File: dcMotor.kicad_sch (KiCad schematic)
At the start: 121 parts, among them J1 USB_C_Receptacle_USB2.0_16P, J2 USB_C_Receptacle_USB2.0_16P, J3 Conn_ST_STDC14, J6 Conn_01x02_Pin, J7 Conn_01x04_Pin, J8 Conn_01x06_Pin, Q1 AO3400A, SW1 SW_Push, SW2 SW_Push, U1 LMR54406DBVR, U10 MCP6561-OT, U11 NUCLEO-L432KC, U2 NCP718ASNADJT1G, U3 NCP718ASNADJT1G, U5 TLV9152IDR, U6 ER_OLEDM0.91_1x-I2C, U7 STM32G431CBTx, U8 LTH-301-05, U9 DRV8231ADDA

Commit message: wip
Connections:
- net +3.3V: now also J7.2 (Pin_2)
- net GND: now also J7.1 (Pin_1)
- net I2C2_SCL: now also J7.3 (Pin_3)
- net I2C2_SDA: now also J7.4 (Pin_4)
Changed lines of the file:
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@@
 	(wire
 		(pts
+			(xy 160.02 59.69) (xy 162.56 59.69)
+		)
+		(stroke
+			(width 0)
+			(type default)
+		)
+	)
+	(wire
+		(pts
 			(xy 294.64 64.77) (xy 304.8 64.77)
 		)
@@
 	(wire
 		(pts
+			(xy 160.02 54.61) (xy 171.45 54.61)
+		)
+		(stroke
+			(width 0)
+			(type default)
+		)
+	)
+	(wire
+		(pts
 			(xy 95.25 250.19) (xy 109.22 250.19)
 		)
@@
 	(wire
 		(pts
+			(xy 160.02 57.15) (xy 170.18 57.15)
+		)
+		(stroke
+			(width 0)
+			(type default)
+		)
+	)
+	(wire
+		(pts
 			(xy 257.81 158.75) (xy 242.57 158.75)
 		)
@@
 	(wire
 		(pts
+			(xy 160.02 52.07) (xy 171.45 52.07)
+		)
+		(stroke
+			(width 0)
+			(type default)
+		)
+	)
+	(wire
+		(pts
 			(xy 81.28 39.37) (xy 91.44 39.37)
 		)
@@
 		)
 	)
+	(label "I2C2_SCL"
+		(at 171.45 54.61 180)
+		(effects
+			(font
+				(size 1.27 1.27)
+			)
+			(justify right bottom)
+		)
+	)
 	(label "SWCLK"
 		(at 257.81 173.99 180)
@@
 		)
 	)
+	(label "I2C2_SDA"
+		(at 171.45 52.07 180)
+		(effects
+			(font
+				(size 1.27 1.27)
+			)
+			(justify right bottom)
+		)
+	)
 	(label "TIM1_CH1"
 		(at 330.2 149.86 0)
@@
 	(symbol
 		(lib_id "Connector:Conn_01x04_Pin")
-		(at 154.94 54.61 0)
+		(at 154.94 57.15 0)
+		(mirror x)
 		(unit 1)
 		(body_style 1)
@@
 		(in_pos_files yes)
 		(dnp yes)
-		(fields_autoplaced yes)
 		(property "Reference" "J7"
-			(at 155.575 46.99 0)
+			(at 155.575 64.77 0)
 			(show_name no)
 			(do_not_autoplace no)
@@
 		)
 		(property "Value" "Conn_01x04_Pin"
-			(at 155.575 49.53 0)
+			(at 155.575 62.23 0)
 			(show_name no)
 			(do_not_autoplace no)
@@
 		)
 		(property "Footprint" "Connector_PinHeader_2.54mm:PinHeader_1x04_P2.54mm_Vertical"
-			(at 154.94 54.61 0)
+			(at 154.94 57.15 0)
 			(hide yes)
 			(show_name no)
@@
 		)
 		(property "Datasheet" "https://jlc-prod-smt.oss-eu-central-1.aliyuncs.com/smtDataManualFile/8590908656076869632-C7430360.pdf?response-content-disposition=attachment%3B%20filename%3DC7430360.pdf%3B%20filename%2A%3DUTF-8%27%27C7430360.pdf&x-oss-date=20260803T060238Z&x-oss-expires=1800&x-oss-security-token=CAISgAN1q6Ft5B2yfSjIr5mMDMrQ3ugT1IisQ0KFpVMBWrtIjbbCoDz2IHhMdHJsAOodtv0%2FmmhT6PkclqRLcbhpcmfjV%2BZHzLB8qYV161ZV4J7b16cNrbH4M4H6aXeirtuwDsz9SNTCALjPD3nPii50x5bjaDymRCbLGJaViJlhHLN1Ow6jdmhpCctxLAlvo9NgFxm3D%2Fu2NQPwiWf9FVdhvhEG6Vly8qOi2MaRmFy8yFTx0b0SvJ%2BjYMrmPctoN9JnSdC5mfdzau3a1TJ84gRD0a5wkaVA1zbDs5bfISEIuUzebreLqY03dV4mOvdqIcMe8qigz88fk%2FfIioH6xyxKOexoSCnFTOiiupCcQLPyao9jLu6iayqViY7QaIOTqQohZmkAMwVOasAsI3Ngh4zF97Qt0cVNkXO9gWfLI8DtuMleWorKE09jitHD0eS19jklBdzSlusJRAJJUVBflCeKEaRNSAd3WGhEfM2%2BBt4QT30w5N2u00S8OSMIzVToo6KWD5sagAFvYbpT7M4nKzV9x9nG0KVt6L9PAQwcrMXPLAqBWLfjjl5RjllW3eVSTNXt%2F6qUNa4JzQr3WbjAO3ylgIsIr1rmH1qmomnc5ro9zTqD80vC%2BHI%2B1cBZ6acWZAaNL8CKJQhHlU474BssQ3TqMWqi0fbuUZIeUyi0gR7g0jSOj3oNhSAA&x-oss-signature-version=OSS4-HMAC-SHA256&x-oss-credential=STS.NZ9Gpd372cJGAd4ASTV4dbsiB%2F20260803%2Feu-central-1%2Foss%2Faliyun_v4_request&x-oss-signature=589712091c6788fe5c51930447157b69597e4cec471ecd001fa8bdaaec699515"
-			(at 154.94 54.61 0)
+			(at 154.94 57.15 0)
 			(hide yes)
 			(show_name no)
@@
 		)
 		(property "Description" "Generic connector, single row, 01x04, script generated"
-			(at 154.94 54.61 0)
+			(at 154.94 57.15 0)
 			(hide yes)
 			(show_name no)
@@
 		)
 		(property "LCSC Part #" "C7430360"
-			(at 154.94 54.61 0)
+			(at 154.94 57.15 0)
 			(hide yes)
 			(show_name no)
@@
 		)
 		(property "FT Rotation Offset" "90"
-			(at 154.94 54.61 0)
+			(at 154.94 57.15 0)
 			(hide yes)
 			(show_name no)
@@
 	(symbol
 		(lib_id "power:GND")
+		(at 162.56 59.69 90)
+		(unit 1)
+		(body_style 1)
+		(exclude_from_sim no)
+		(in_bom yes)
+		(on_board yes)
+		(in_pos_files yes)
+		(dnp no)
+		(property "Reference" "#PWR0100"
+			(at 168.91 59.69 0)
+			(hide yes)
+			(show_name no)
+			(do_not_autoplace no)
+			(effects
+				(font
+					(size 1.27 1.27)
+				)
+			)
+		)
+		(property "Value" "GND"
+			(at 166.37 59.69 0)
+			(show_name no)
+			(do_not_autoplace no)
+			(effects
+				(font
+					(size 1.27 1.27)
+				)
+			)
+		)
+		(property "Footprint" ""
+			(at 162.56 59.69 0)
+			(hide yes)
+			(show_name no)
+			(do_not_autoplace no)
+			(effects
+				(font
+					(size 1.27 1.27)
+				)
+			)
+		)
+		(property "Datasheet" ""
+			(at 162.56 59.69 0)
+			(hide yes)
+			(show_name no)
+			(do_not_autoplace no)
+			(effects
+				(font
+					(size 1.27 1.27)
+				)
+			)
+		)
+		(property "Description" "Power symbol creates a global label with name \"GND\" , ground"
+			(at 162.56 59.69 0)
+			(hide yes)
+			(show_name no)
+			(do_not_autoplace no)
+			(effects
+				(font
+					(size 1.27 1.27)
+				)
+			)
+		)
+		(pin "1"
+		)
+		(instances
+			(project "dcMotor"
+				(path "/cdbcf673-237a-45f1-99a3-f4d168bf6e2e"
+					(reference "#PWR0100")
+					(unit 1)
+				)
+			)
+		)
+	)
+	(symbol
+		(lib_id "power:GND")
 		(at 196.85 24.13 90)
 		(unit 1)
@@
 					(unit 1)
 				)
+			)
+		)
+	)
+	(symbol
+		(lib_id "power:+3.3V")
+		(at 170.18 57.15 270)
+		(unit 1)
+		(body_style 1)
+		(exclude_from_sim no)
+		(in_bom yes)
+		(on_board yes)
+		(in_pos_files yes)
+		(dnp no)
+		(property "Reference" "#PWR0101"
+			(at 166.37 57.15 0)
+			(hide yes)
+			(show_name no)
+			(do_not_autoplace no)
+			(effects
+				(font
+					(size 1.27 1.27)
+				)
+			)
+		)
+		(property "Value" "+3.3V"
+			(at 173.99 57.15 0)
+			(show_name no)
+			(do_not_autoplace no)
+			(effects
+				(font
+					(size 1.27 1.27)
+				)
+			)
+		)
+		(property "Footprint" ""
+			(at 170.18 57.15 0)
+			(hide yes)
+			(show_name no)
+			(do_not_autoplace no)
+			(effects
+				(font
+					(size 1.27 1.27)
+				)
+			)
+		)
+		(property "Datasheet" ""
+			(at 170.18 57.15 0)
+			(hide yes)
+			(show_name no)
+			(do_not_autoplace no)
+			(effects
+				(font
+					(size 1.27 1.27)
+				)
+			)
+		)
+		(property "Description" "Power symbol creates a global label with name \"+3.3V\""
+			(at 170.18 57.15 0)
+			(hide yes)
+			(show_name no)
+			(do_not_autoplace no)
+			(effects
+				(font
+					(size 1.27 1.27)
+				)
+			)
+		)
+		(pin "1"
+		)
+		(instances
+			(project "dcMotor"
+				(path "/cdbcf673-237a-45f1-99a3-f4d168bf6e2e"
+					(reference "#PWR0101")
+					(unit 1)
+				)

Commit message: cleanup
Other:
- note added: "TIM2 configured in CubeMX as "combined channels" in Encoder Mode to measure Motor Hall Encoder Signals"
- moved on the sheet: C27, C32, C33, D7, J8, NT1, NT2, R25, R26, R30, R31, TP11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

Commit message: cleanup
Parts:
- added C39, C40: 100n, Capacitor_SMD:C_0402_1005Metric, symbol Device:C
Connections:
- net +3.3V: now also C39.2, C40.2
- net GND: now also C39.1, C40.1
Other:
- note added: "more caps than necessary due to "bad" routing"

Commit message: fabrication
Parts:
- U1, U10, U5: now not fitted
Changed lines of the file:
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@@
 		(on_board yes)
 		(in_pos_files yes)
-		(dnp no)
+		(dnp yes)
 		(property "Reference" "U1"
 			(at 52.07 28.702 0)
@@
 		(on_board yes)
 		(in_pos_files yes)
-		(dnp no)
+		(dnp yes)
 		(property "Reference" "U10"
 			(at 374.904 49.53 0)
@@
 		(on_board yes)
 		(in_pos_files yes)
-		(dnp no)
+		(dnp yes)
 		(property "Reference" "U5"
 			(at 116.84 243.332 0)
@@
 		(on_board yes)
 		(in_pos_files yes)
-		(dnp no)
+		(dnp yes)
 		(fields_autoplaced yes)
 		(property "Reference" "U5"
@@
 		(on_board yes)
 		(in_pos_files yes)
-		(dnp no)
+		(dnp yes)
 		(property "Reference" "U5"
 			(at 180.34 243.332 0)

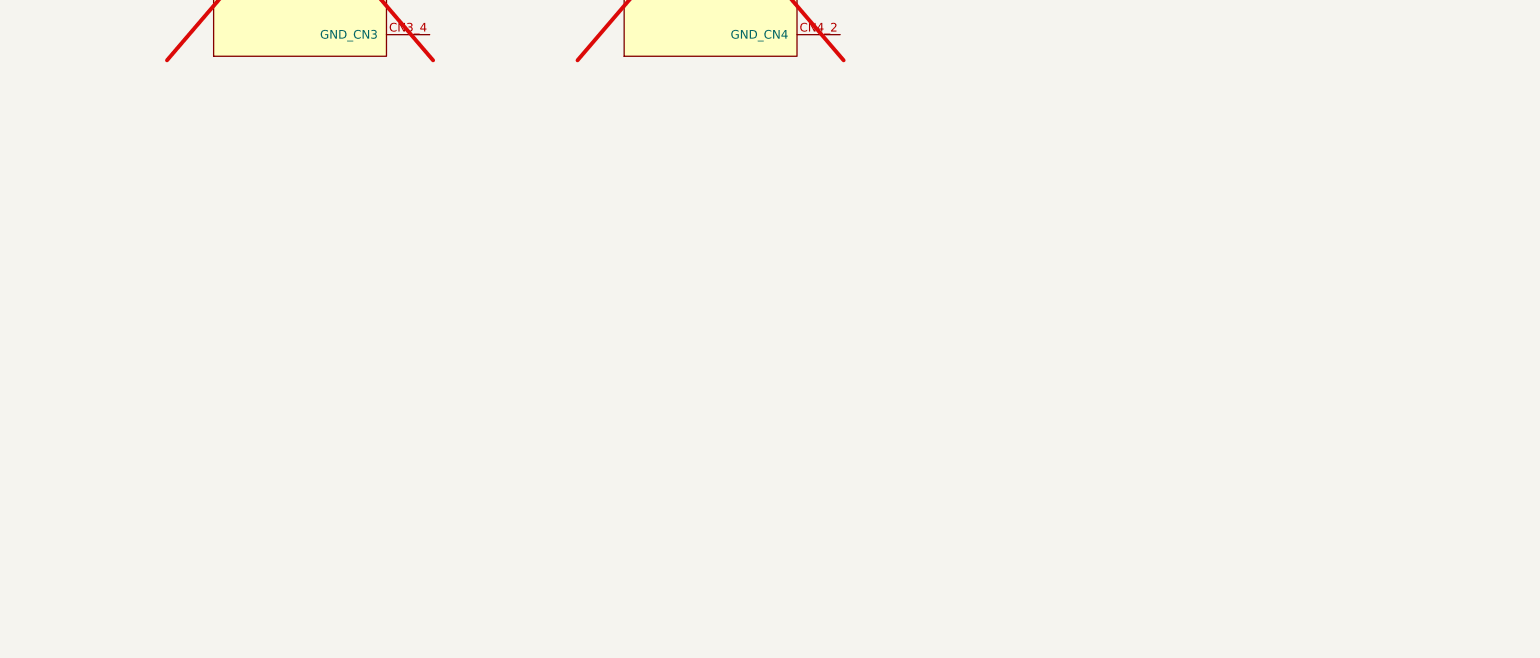
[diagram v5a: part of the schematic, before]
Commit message: footprint for 64 pin nucleo on the bottom side
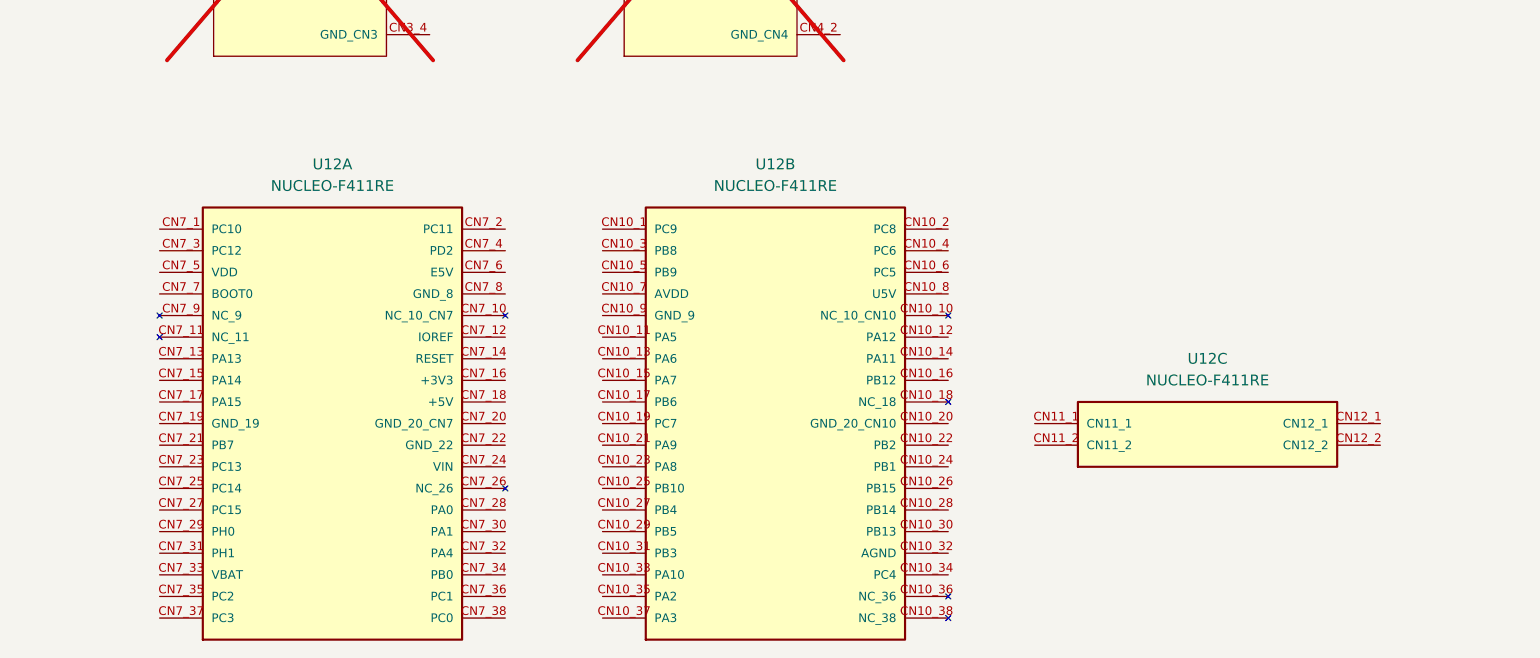
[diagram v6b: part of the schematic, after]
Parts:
- added U12: NUCLEO-F411RE, BOARD_NUCLEO-F411RE, symbol NUCLEO-F411RE:NUCLEO-F411RE

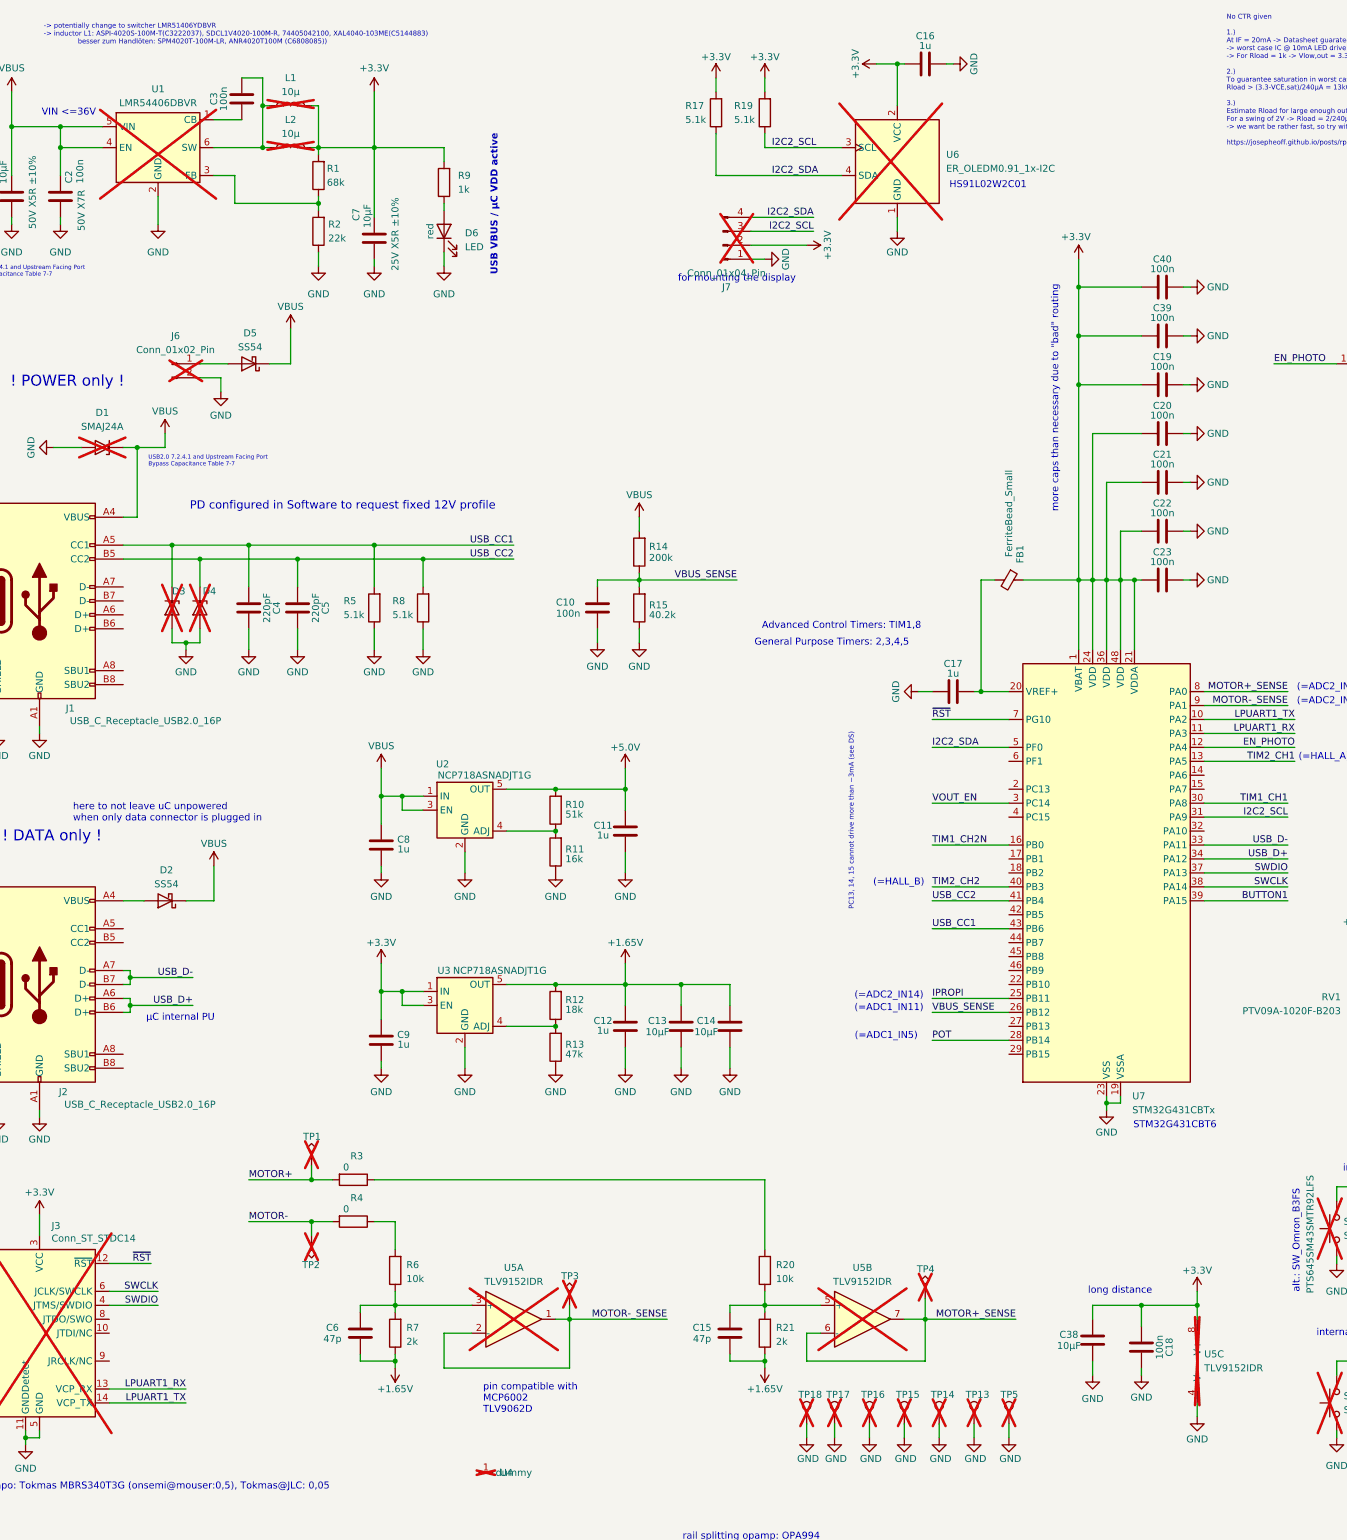
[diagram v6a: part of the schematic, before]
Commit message: changed opamp supply from 3V3 to 5V to avoid cross-over distortion
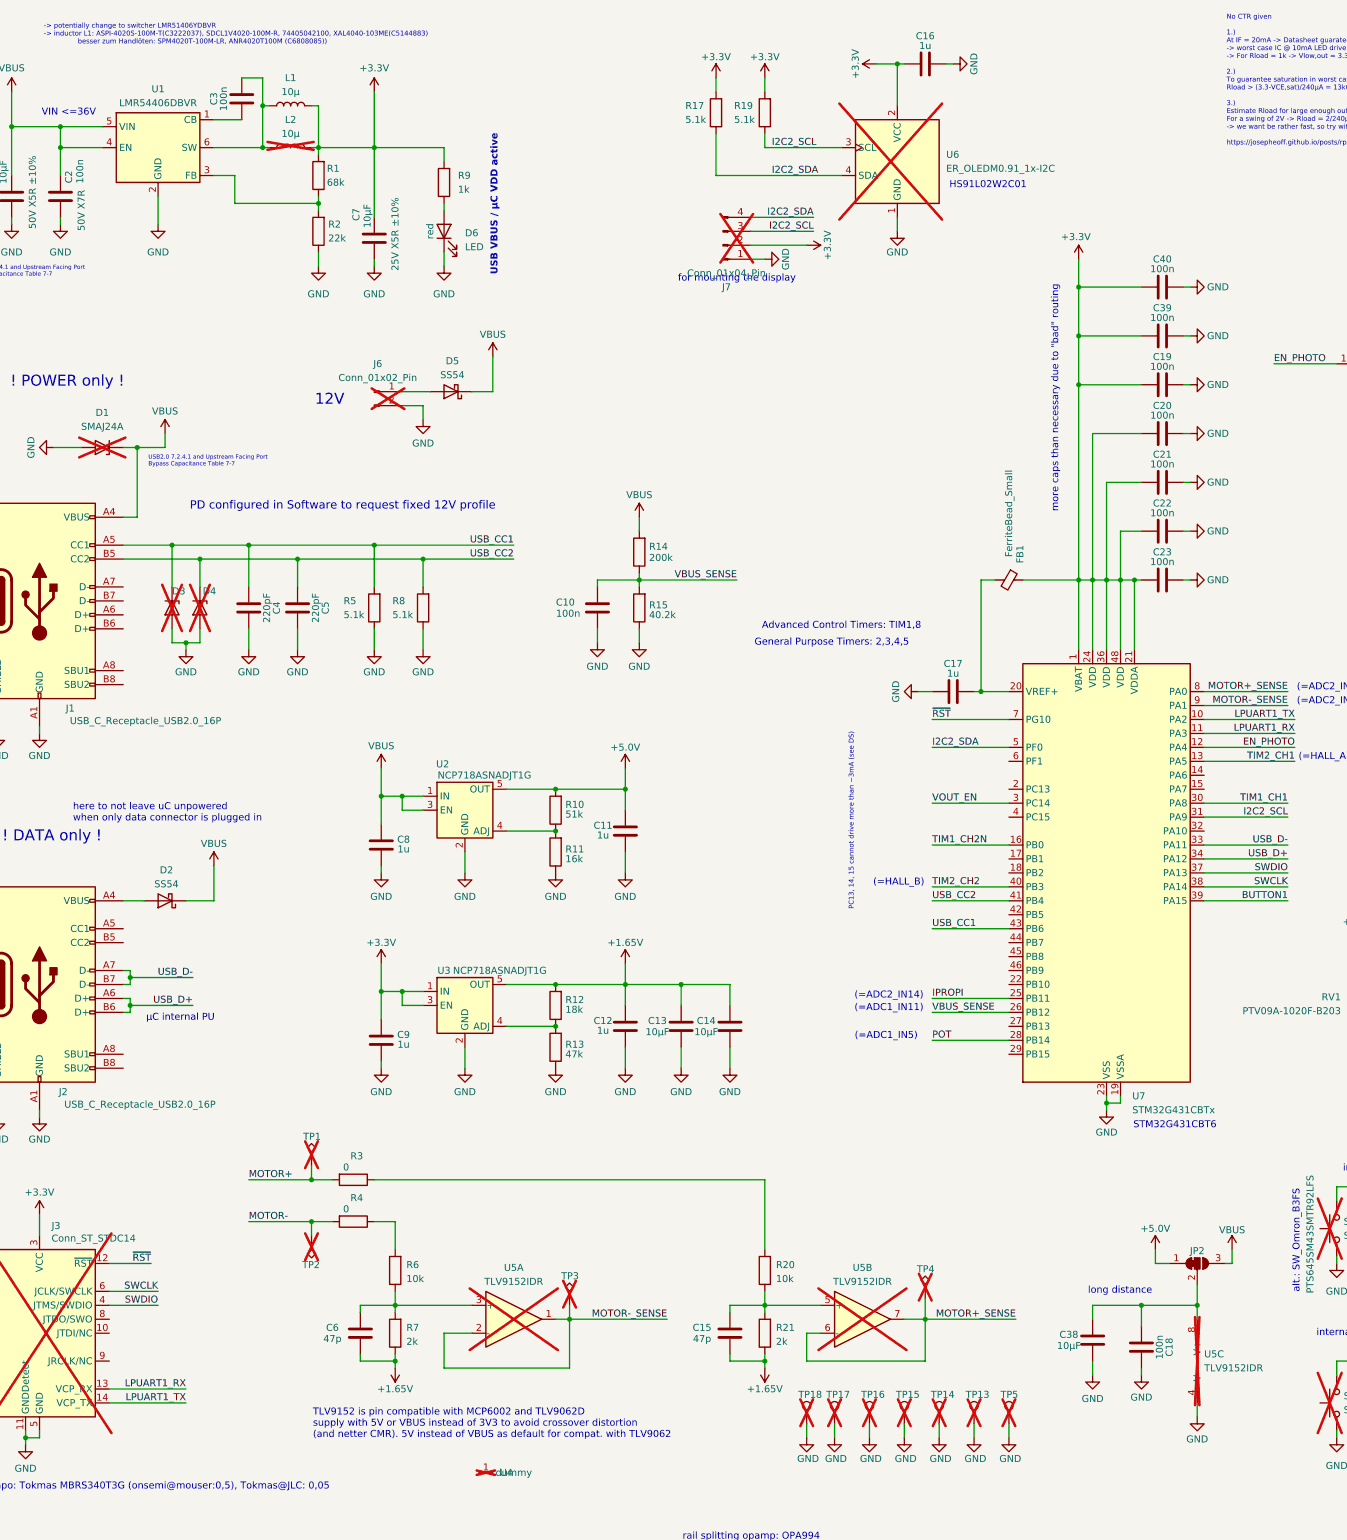
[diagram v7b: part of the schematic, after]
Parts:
- added JP2: SolderJumper_3_Bridged12, Jumper:SolderJumper-3_P1.3mm_Bridged12_RoundedPad1.0x1.5mm_NumberLabels, symbol Jumper:SolderJumper_3_Bridged12
- L1, U1: now fitted
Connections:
- net +3.3V: no longer C18.2, C38.2, U5.8 (V+)
- net +5.0V: now also JP2.1 (A)
- net VBUS: now also JP2.3 (B)
- new net: C18.2, C38.2, JP2.2 (C), U5.8 (V+)
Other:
- note added: "12V"
- note added: "TLV9152 is pin compatible with MCP6002 and TLV9062D supply with 5V or VBUS instead of 3V3 to avoid crossover distortion (and netter CMR). 5V instead of VBUS as default for compat. with TLV9062"
- note removed: "pin compatible with MCP6002 TLV9062D"
- moved on the sheet: D5, J6
